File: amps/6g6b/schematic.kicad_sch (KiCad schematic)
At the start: 92 parts, among them T1 125P7A, T3 125A13A

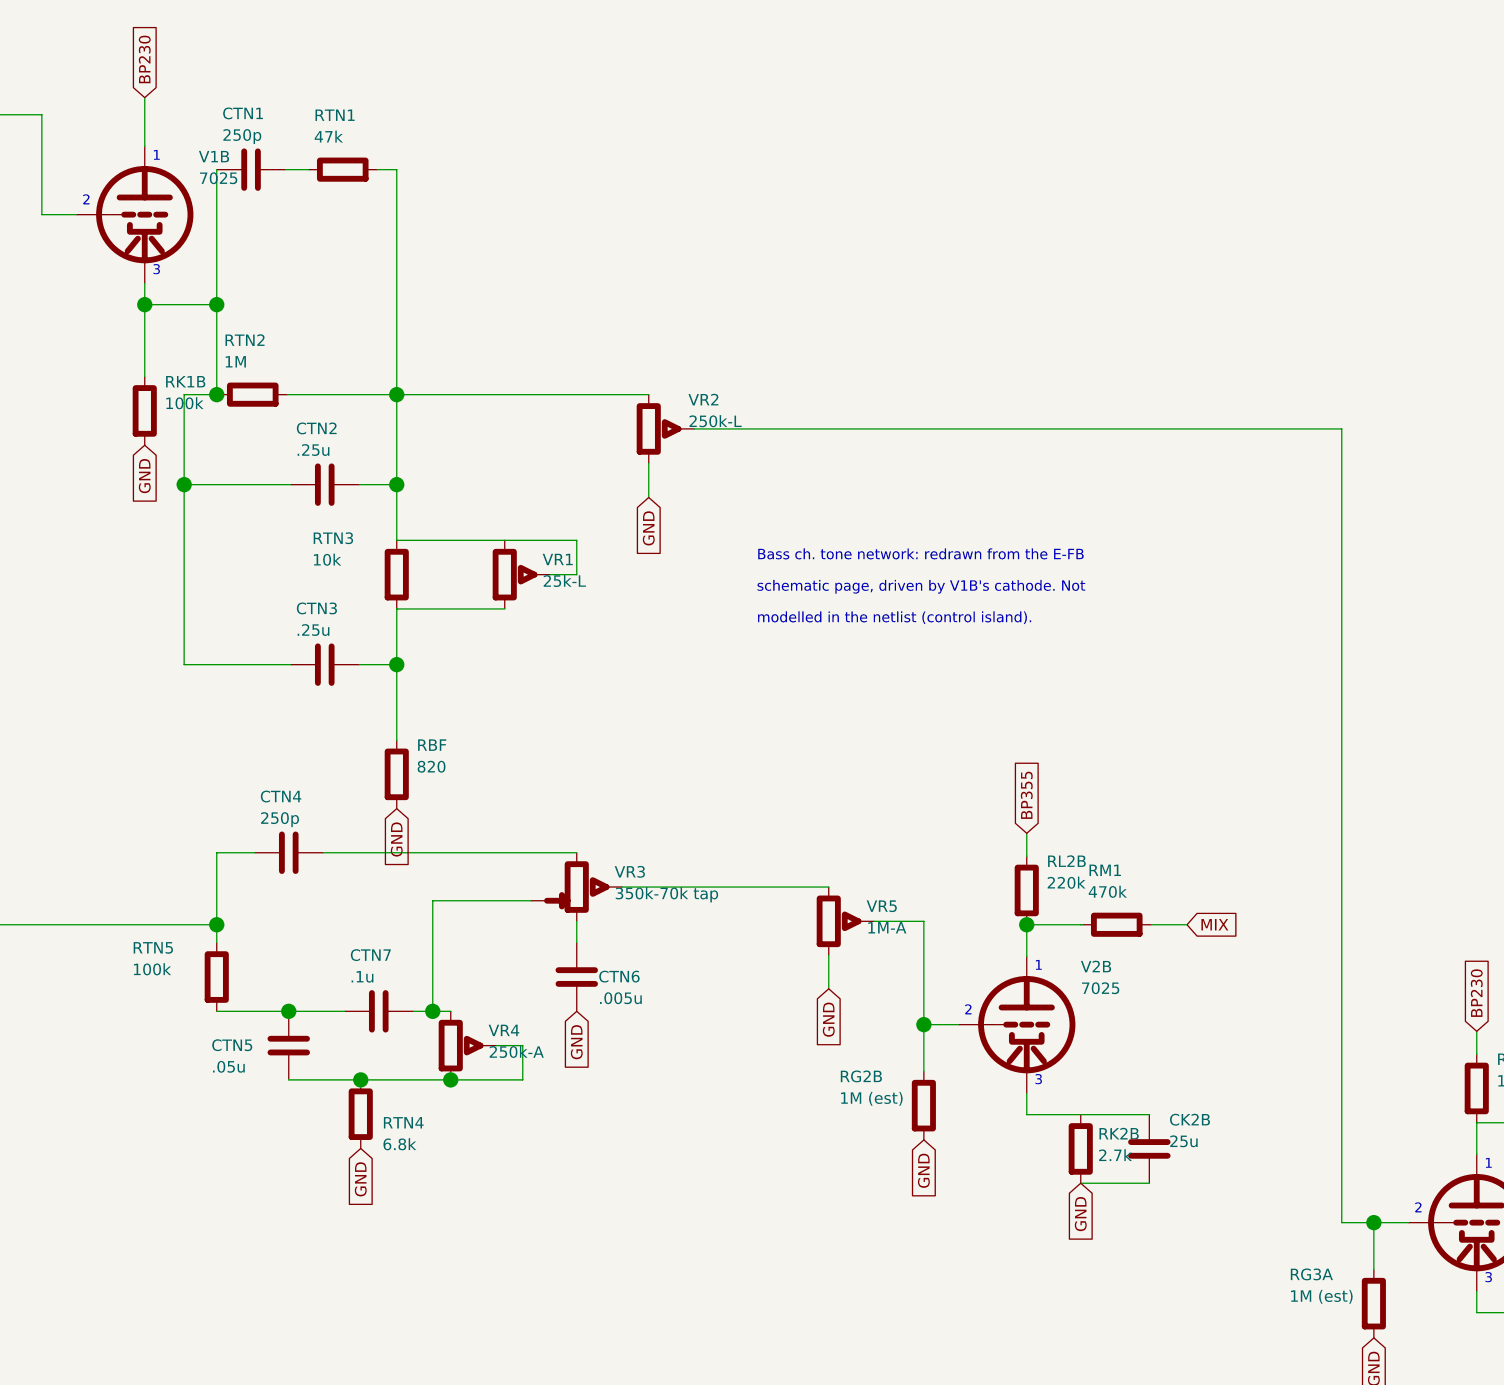
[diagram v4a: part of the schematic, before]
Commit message: Fix: the 6G6-B Bass-channel tone network, on both the sheet and the board
Both E-FB pages draw one network: V1B's cathode (A) -> .00025 -> 47k -> the Volume pot's top (T); A -> 1M -> X; X -> .25 -> B and X -> .25 -> C; T -> 10k -> B; the 25K-L Bass rheostat from B (wiper) to C (its far lug); C -> 820 -> ground. Schematic page crop (900,550)-(2100,1850); layout page crops (5000,1750)-(6300,2800) for the board and (4300,450)-(5700,1200) for the pots.

The sheet put the 1M in parallel with the .00025+47k branch, ran both .25s from the 1M's foot, and drew the Bass pot across the 10k. The board chained the parts and left the Bass wiper unwired. Both are redrawn to the network above, with every part lying along the grid. The sheet-board gate's 6G6-B misplaced list goes from [CTN2, CTN3] to [].

Read from the layout page:
- The 820 sits inside the Bass pot's circle, from the left lug to ground, and is nowhere on the board. RBF is now an off-board part at VR1, like the Normal channel's 6800 at its own Bass pot.
- The Bass pot's third (right) lug is bare: no strap and no lead at 3x zoom of crop (4380,500)-(4750,800). VR1 therefore wires lug 1 (C) and lug 2 (B), and lug 3 is free on both surfaces. sch_open_pins.yaml waives VR1.3 the way it waives the 6161 and GA-40 rheostats.
- The Bass Volume's grounded lug is the left one. This board already reads a factory-left lug as lug 1 (VR3.lug1 takes the .005 bleed and VR4.lug1 the 6800 foot, both drawn on the left lug), and a lug-1 ground makes the Volume turn up clockwise. So VR2's lug 1 to ground and lug 3 to T already match the factory, and VR2 is unchanged.

bom.yaml roles for CTN1-3, RTN1-3, VR1 and RBF, the notes.md paragraph, and the net_map RTN3/RBF notes now describe this topology instead of the old parallel one. No value changes. The network stays outside netlist.cir. Both board drawings, the site copies and the og card are regenerated. FW-19 P10c.

Co-Authored-By: Claude Opus 5.5 <noreply@anthropic.com>
Claude-Session: ht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
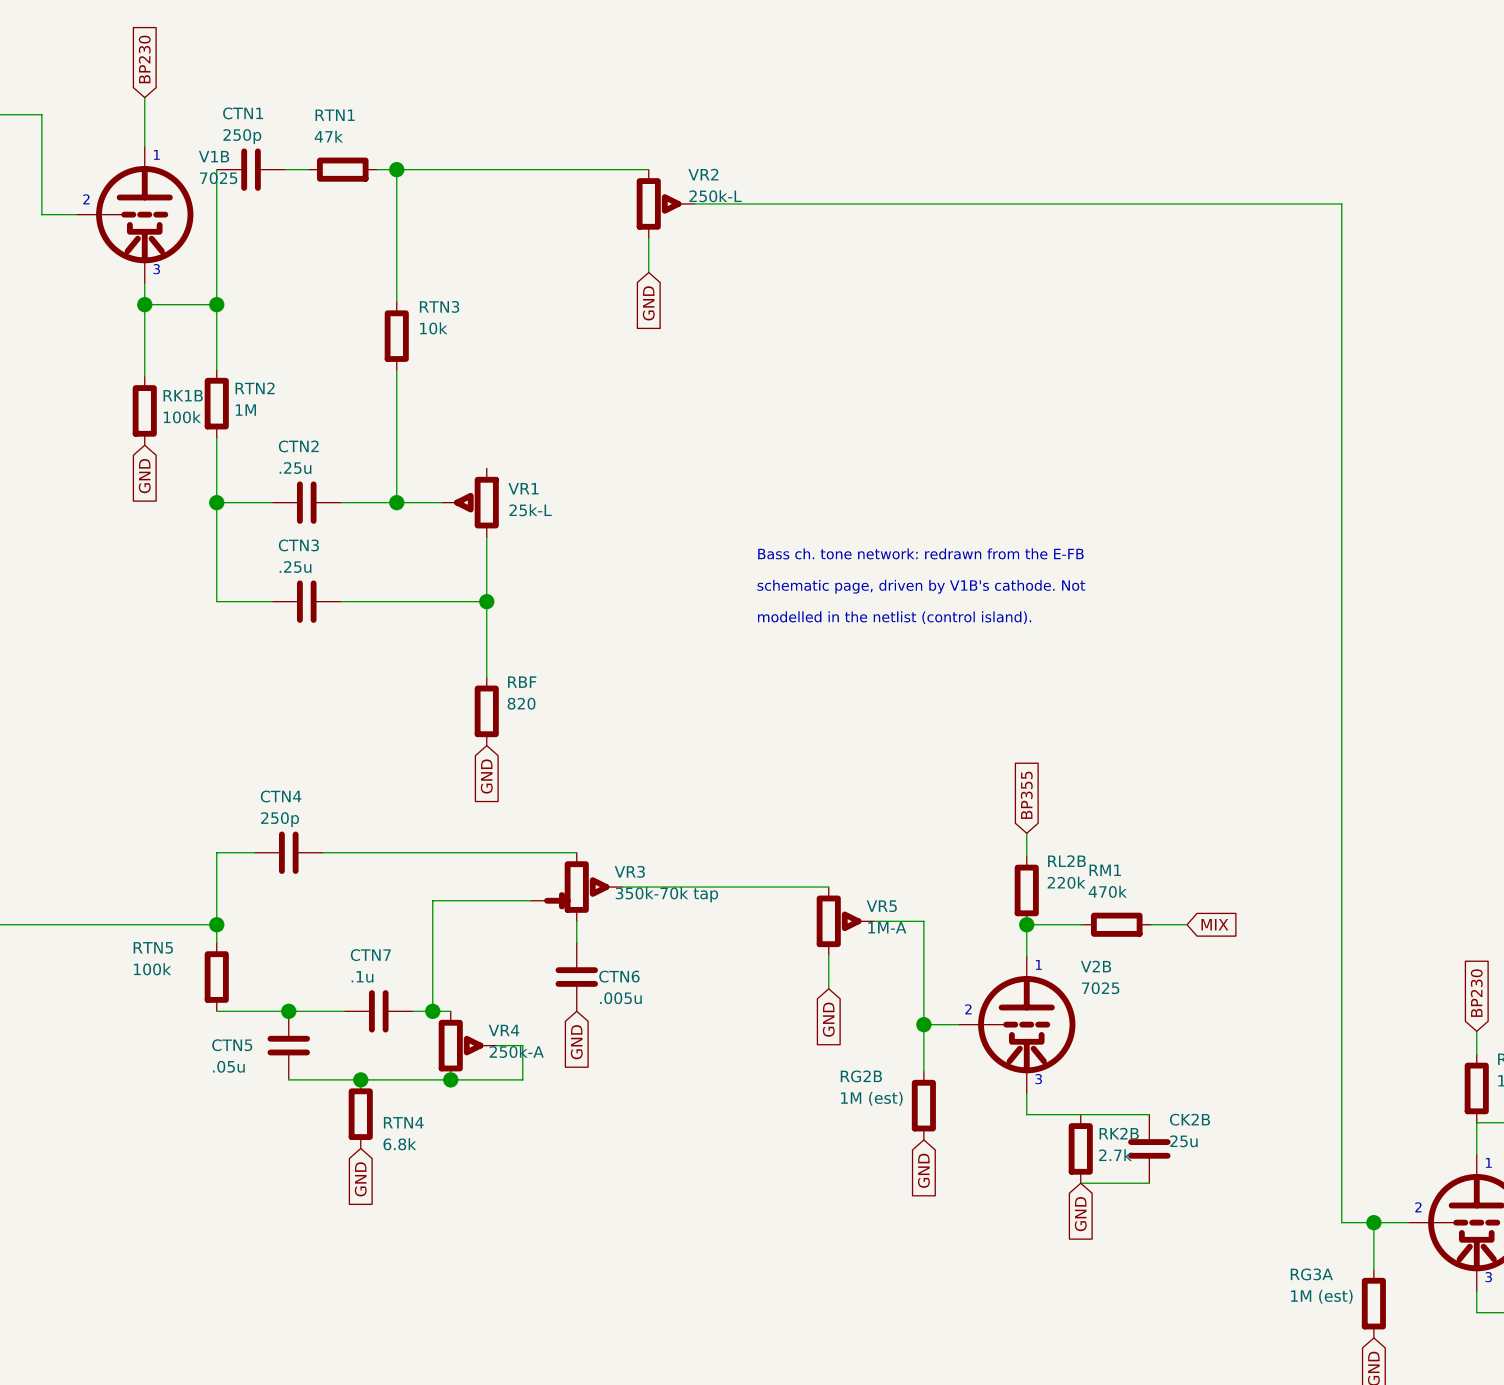
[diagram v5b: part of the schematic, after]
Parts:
- removed C1: 500p, symbol cx:C
- removed C12: 20u 600V, symbol cx:C
- removed CTN7: .1u, symbol cx:C
- removed DB1: 1N4148, symbol cx:DIODE_SS
- removed DR1: 1N4007, symbol cx:DIODE_SS
- removed R4s: 68k, symbol cx:R
- removed RB1: 1k 1W 5%, symbol cx:R
- removed RD1: 4.7k 1W, symbol cx:R
- removed RG2B: 1M (est), symbol cx:R
- removed RG4A, RTN2: 1M, symbol cx:R
- removed RGL5, RGL6: 220k, symbol cx:R
- removed RL3A, RL3B: 100k, symbol cx:R
- removed RS6: 470 1W, symbol cx:R
- removed RTN4: 6.8k, symbol cx:R
- removed V4A: 7025, symbol cx:TRIODE
- removed VR3: 350k-70k tap, symbol cx:POT_TAP
- added C10, C14: 20u 600V, symbol cx:C
- added CTN1, CTN4: 250p, symbol cx:C
- added CTN5: .05u, symbol cx:C
- added L1: 125C1A, symbol cx:CHOKE
- added RD3: 56k 1W, symbol cx:R
- added RG3A: 1M (est), symbol cx:R
- added RK3B: 1.5k, symbol cx:R
- added RL2A: 100k, symbol cx:R
- added RL2B: 220k, symbol cx:R
- added RM2: 470k, symbol cx:R
- added RPF: 4.7k, symbol cx:R
- added T1: 125P7A, symbol cx:PT
- added V2A, V2B: 7025, symbol cx:TRIODE
- added V5, V6: 5881, symbol cx:PENTODE
- added VR7: 25k-L · Presence, symbol cx:POT
- C1: renamed from RK3B; value 1.5k -> 500p; symbol cx:R -> cx:C
- CTN7: renamed from CTN4; value 250p -> .1u
- DB1: renamed from C14; value 20u 600V -> 1N4148; symbol cx:C -> cx:DIODE_SS
- DR1: renamed from T1; value 125P7A -> 1N4007; symbol cx:PT -> cx:DIODE_SS
- R4s: renamed from V2A; value 7025 -> 68k; symbol cx:TRIODE -> cx:R
- RB1: renamed from RD3; value 56k 1W -> 1k 1W 5%
- RD1: renamed from L1; value 125C1A -> 4.7k 1W; symbol cx:CHOKE -> cx:R
- RG2B: renamed from V2B; value 7025 -> 1M (est); symbol cx:TRIODE -> cx:R
- RG3B: renamed from VR6; value 250k-A · Bass Treble -> 1M (est); symbol cx:POT -> cx:R
- RG4A: renamed from RPF; value 4.7k -> 1M
- RGL5: renamed from VR7; value 25k-L · Presence -> 220k; symbol cx:POT -> cx:R
- RGL6: renamed from RS5; value 470 1W -> 220k
- RK3A: renamed from V3A; value 7025 -> 1.5k (est); symbol cx:TRIODE -> cx:R; Basing_unit 2 -> (none)
- RL3A: renamed from RG3A; value 1M (est) -> 100k
- RL3B: renamed from RG3B; value 1M (est) -> 100k
- RS5: renamed from V5; value 5881 -> 470 1W; symbol cx:PENTODE -> cx:R
- RS6: renamed from V6; value 5881 -> 470 1W; symbol cx:PENTODE -> cx:R
- RTN2: renamed from CTN1; value 250p -> 1M; symbol cx:C -> cx:R
- RTN4: renamed from CTN5; value .05u -> 6.8k; symbol cx:C -> cx:R
- V3A: renamed from RL2B; value 220k -> 7025; symbol cx:R -> cx:TRIODE; Basing_unit (none) -> 2
- V4A: renamed from RM2; value 470k -> 7025; symbol cx:R -> cx:TRIODE; Basing_unit (none) -> 2
- VR3: renamed from RL2A; value 100k -> 350k-70k tap; symbol cx:R -> cx:POT_TAP
- VR6: renamed from RK3A; value 1.5k (est) -> 250k-A · Bass Treble; symbol cx:R -> cx:POT
- renumbered C10 to C11, C11 to C12
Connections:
- net BP230: now also RL3A.1, RL3B.1, C14.1, RD3.2; no longer DB1.1, RB1.2
- net BP355: now also RL2A.1, RL2B.1; no longer V3A.1, VR3.1
- net BP410: now also C12.1, RD1.2
- net BP428: now also C11.1, RD1.1, RS5.2, RS6.2, L1.2, RD3.1; no longer C12.1, RB1.1, RD1.2, RGL6.2
- net BP430: now also C10.1, L1.1; no longer C11.1, RD1.1
- net GND: now also RG2B.2, RG3B.2, RK3A.2, RTN4.2, VR6.3, C10.2, C14.2, RG3A.2, RK3B.2, RPF.2, T1.4 (HT_CT), V5.4 (K), V6.4 (K), VR7.3; no longer C1.2, DB1.2, DR1.4 (HT_CT), RG3B.3, RG4A.2, RGL5.3, RL3A.2, RL3B.2, RS5.4 (K), RS6.4 (K), VR6.2
- net HT_A: now also DR1.1 (A), T1.3 (HT_A); no longer DR1.3 (HT_A)
- net HT_B: now also T1.5 (HT_B); no longer DR1.5 (HT_B)
- net HT_TAP: now also RB1.1, T1.6 (HT_TAP); no longer DR1.6 (HT_TAP)
- net MIX: now also C1.1, RM2.2; no longer V4A.2
- net NBIAS: now also DB1.1 (A), RGL5.2, RGL6.2
- net NORM1: now also R4s.1
- net at RTN1.2, RTN3.1, VR2.1: no longer CTN2.2, VR1.1, VR1.2 (W)
- net at CK2B.1, RK2B.1: now also V2B.3 (K); no longer RG2B.3 (K)
- net at RNFB.2, RT2.2: now also RPF.1, VR7.1; no longer RG4A.1, RGL5.1
- net at V4A.1 (P): now also C2.1, RL4A.2; no longer V3B.1 (P)
- net at V3B.3 (K): now also RK3B.1; no longer C1.1
- net at RTAIL.1, V4B.3 (K): now also V4A.3 (K)
- net at VR4.1: now also CTN7.2, VR3.4 (T)
- net at VR4.2 (W), VR4.3: now also RTN4.1, CTN5.2; no longer RTN4.2
- net at VR5.1: now also VR3.2 (W)
- net at CTN6.1: now also VR3.3
- net at RK1B.1, RTN2.1, V1B.3 (K): now also CTN1.1; no longer CTN2.1, CTN3.1
- net at C2.2: now also RGL5.1, V5.2 (G1); no longer RS5.2 (G1)
- net at RG4B.2, RT2.1, RTAIL.2: now also RG4A.2
- net at DR2.1 (A): now also DR1.2 (K)
- net at RTN2.2: now also CTN2.1, CTN3.1; no longer RTN1.1
- net at T3.1 (PRI_A): now also V5.1 (P); no longer RS5.1 (P)
- net at T3.3 (PRI_B): now also V6.1 (P); no longer RS6.1 (P)
- net at RTN5.2: now also CTN7.1, CTN5.1; no longer RTN4.1
- net at RGL6.1: now also C3.2, V6.2 (G1); no longer RS5.3 (G2)
- net at CDR1.1: now also RL3A.2, V3A.1 (P); no longer RK3A.1 (P)
- net at VR5.2 (W): now also RG2B.1, V2B.2 (G); no longer RG2B.2 (G)
- net at CK2A.1, RK2A.1: now also V2A.3 (K); no longer R4s.3 (K)
- net at RBF.1: now also CTN3.2, VR1.1
- net at R3s.2, R4s.2, RG2A.1: now also V2A.2 (G)
- net at VR6.1: now also CDR1.2; no longer RK3A.3 (K)
- net at RG3B.1: now also V3B.2 (G), VR6.2 (W); no longer CDR1.2
- new net: RL2B.2, RM1.1, V2B.1 (P)
- new net: C1.2, RG4A.1, V4A.2 (G)
- new net: CTN2.2, RTN3.2, VR1.2 (W)
- new net: RG3A.1, V3A.2 (G), VR2.2 (W)
- new net: RL3B.2, RM2.1, V3B.1 (P)
- new net: CTN4.1, RL2A.2, RTN5.1, V2A.1 (P)
- new net: RS6.1, V6.3 (G2)
- new net: CTN4.2, VR3.1
- new net: RK3A.1, V3A.3 (K)
- new net: DB1.2 (K), RB1.2
- new net: RS5.1, V5.3 (G2)
- new net: CTN1.2, RTN1.1
- now unconnected: VR1.3
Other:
- moved on the sheet: C11, C12, CTN7, DB1, RB1, RG4A, RGL6, RL3A, RL3B
